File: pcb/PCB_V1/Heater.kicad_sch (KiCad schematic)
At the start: 8 parts, among them J601 PTC + / switched - (3.5 mm), Q601 NTMFS5C628NLT1G, U601 UCC27524ADR

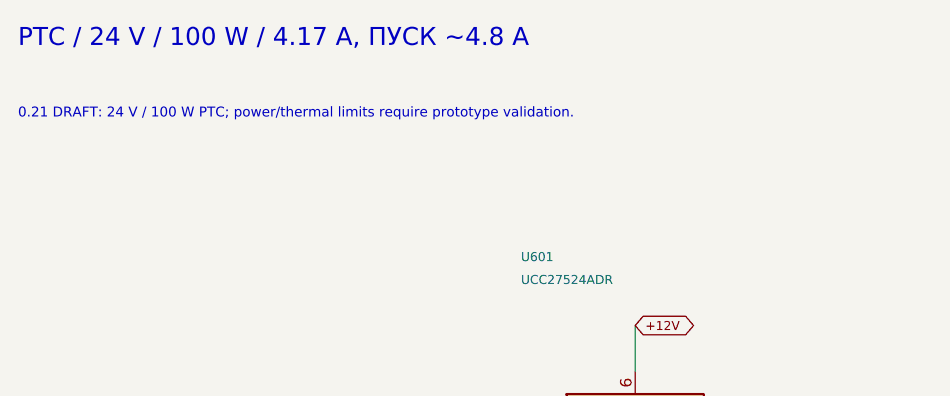
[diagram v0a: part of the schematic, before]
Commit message: pcb: revision 0.22 routing preparation
- Stack confirmed by the user: 1.6 mm, 1 oz outer, 0.5 oz inner.
- LED output MLCCs: Murata GRM32EC72A106KE05L (X7S, 50k in stock) instead
  of TDK; DC-bias digitised from Murata data (2.60 uF at 49 V, model
  2.55 uF), CH1 bank 6.44 uF effective.
- microSD: HRO TF-01A (push-push, C91145) on a project footprint from the
  HRO drawing, checked against the LCSC land; SD passives re-placed.
- TP301 on the PCF8563 CLKOUT for crystal trimming.
- Kelvin net ties NT711/NT712/NT721/NT722 at the LED-driver shunts
  (LED*_CS_K, LED*_FB_K); net ties are excluded from the BOM export.
- analyze_copper.py: IPC-2221 copper screen for the confirmed stack
  (main 24 V path needs pours on both outer layers, via counts).
- L711 and XT60PW-M re-checked and kept; reports v22 and ROUTING_PREP.md.
  USD 30.04 per board (28.42 for five), ERC 0, DRC 0.

Co-Authored-By: Claude Opus 5.5 <noreply@anthropic.com>
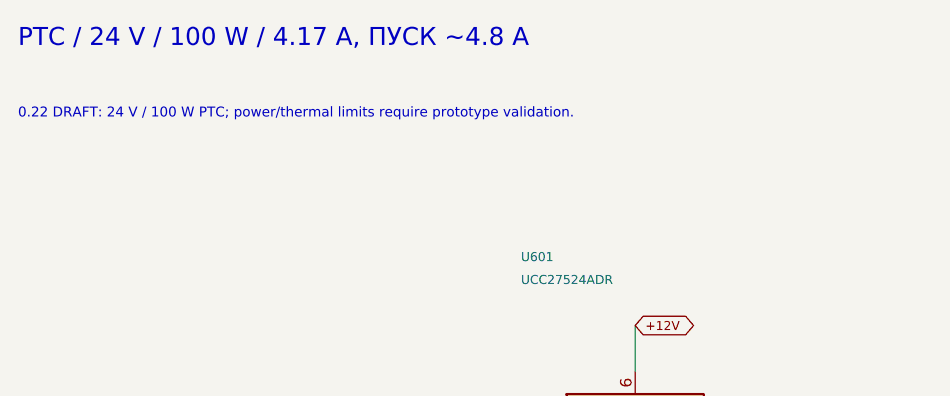
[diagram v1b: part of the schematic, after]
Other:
- note added: "0.22 DRAFT: 24 V / 100 W PTC; power/thermal limits require prototype validation."
- note removed: "0.21 DRAFT: 24 V / 100 W PTC; power/thermal limits require prototype validation."
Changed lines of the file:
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@@
 		(title "05 - PTC heater switch (24 V)")
 		(date "2026-09-30")
-		(rev "0.21-DRAFT")
+		(rev "0.22-DRAFT")
 		(company "GrowBox controller")
 		(comment 1 "Simplified prototype; unrouted; hardware qualification pending")
@@
 		)
 	)
-	(text "0.21 DRAFT: 24 V / 100 W PTC; power/thermal limits require prototype validation."
+	(text "0.22 DRAFT: 24 V / 100 W PTC; power/thermal limits require prototype validation."
 		(exclude_from_sim no)
 		(at 20.32 24.13 0)
